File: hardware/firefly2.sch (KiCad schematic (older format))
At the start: 18 parts, among them J2 614105150721, J3 CONN_01X01, P3 CONN_01X04, P4 CONN_01X05, P5 CONN_01X01, U1 SAMD21E18, U2 RFM69CW, U3 MIC5504

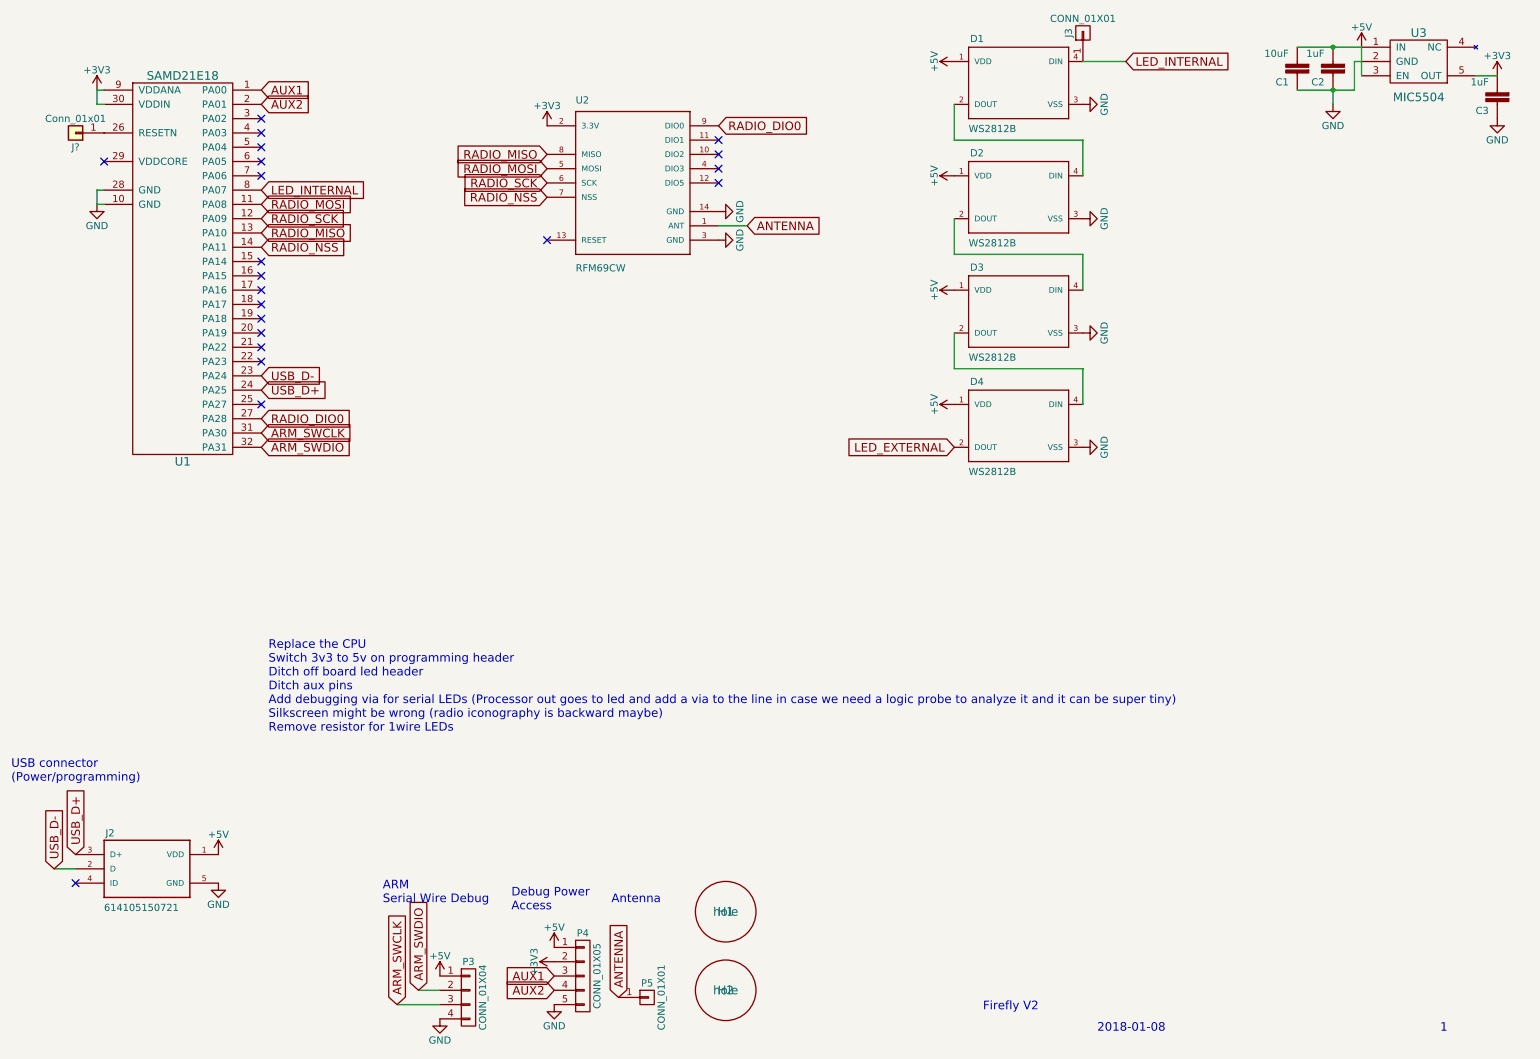
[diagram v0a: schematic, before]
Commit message: Hardware revision 2.4:
- Add buffer to bump LED signal to input voltage
- Add pads between reset and ground, to facilitate testing

Change-Id: If3ba1aed20585e03bd6f188c24cdaebd21a51b41
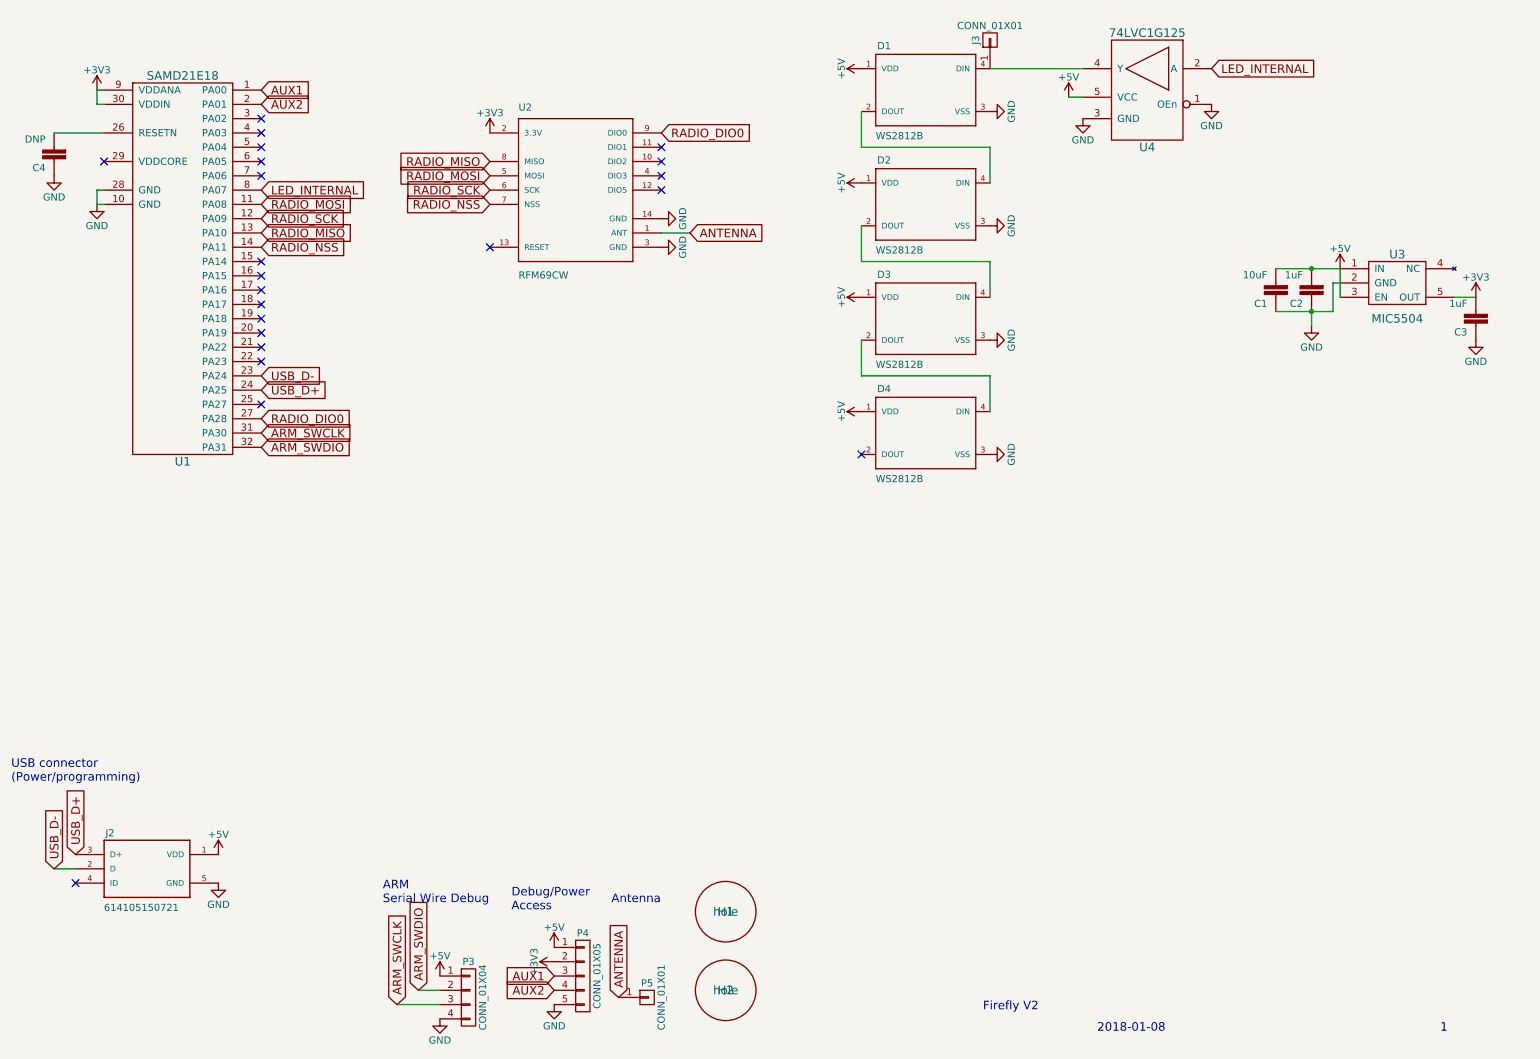
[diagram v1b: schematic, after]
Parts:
- removed J?: Conn_01x01, symbol Conn_01x01
- added C4: DNP, SparkFun-Capacitors:0603, symbol CAP0603-CAP
- added U4: 74LVC1G125, TO_SOT_Packages_SMD:SOT-353_SC-70-5, symbol 74LVC1G125
- J3: footprint (none) -> Pin_Headers:Pin_Header_Straight_1x01_Pitch1.27mm
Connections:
- net +5V: now also U4.5 (VCC)
- net GND: now also C4.1, U4.1 (OEn), U4.3 (GND)
- net LED_INTERNAL: now also U4.2 (A); no longer D1.4 (DIN), J3.1 (P1)
- net at U1.26 (RESETN): now also C4.2
- net LED_EXTERNAL: no longer names the net of D4.2 (DOUT)
- new net: D1.4 (DIN), J3.1 (P1), U4.4 (Y)
- no-connect marks 21 -> 22
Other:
- note added: "Debug/Power\nAccess"
- note removed: "Debug Power\nAccess"
- note removed: "Replace the CPU\nSwitch 3v3 to 5v on programming header\nDitch off board led header\nDitch aux pins\nAdd debugging via for serial LEDs (Processor out goes to led and add a via to the line in case we need a logic probe to analyze it and it can be super tiny)\nSilkscreen might be wrong (radio iconography is backward maybe)\nRemove resistor for 1wire LEDs\n"
- moved on the sheet: C1, C2, C3, D1, D2, D3, D4, J3, U2, U3

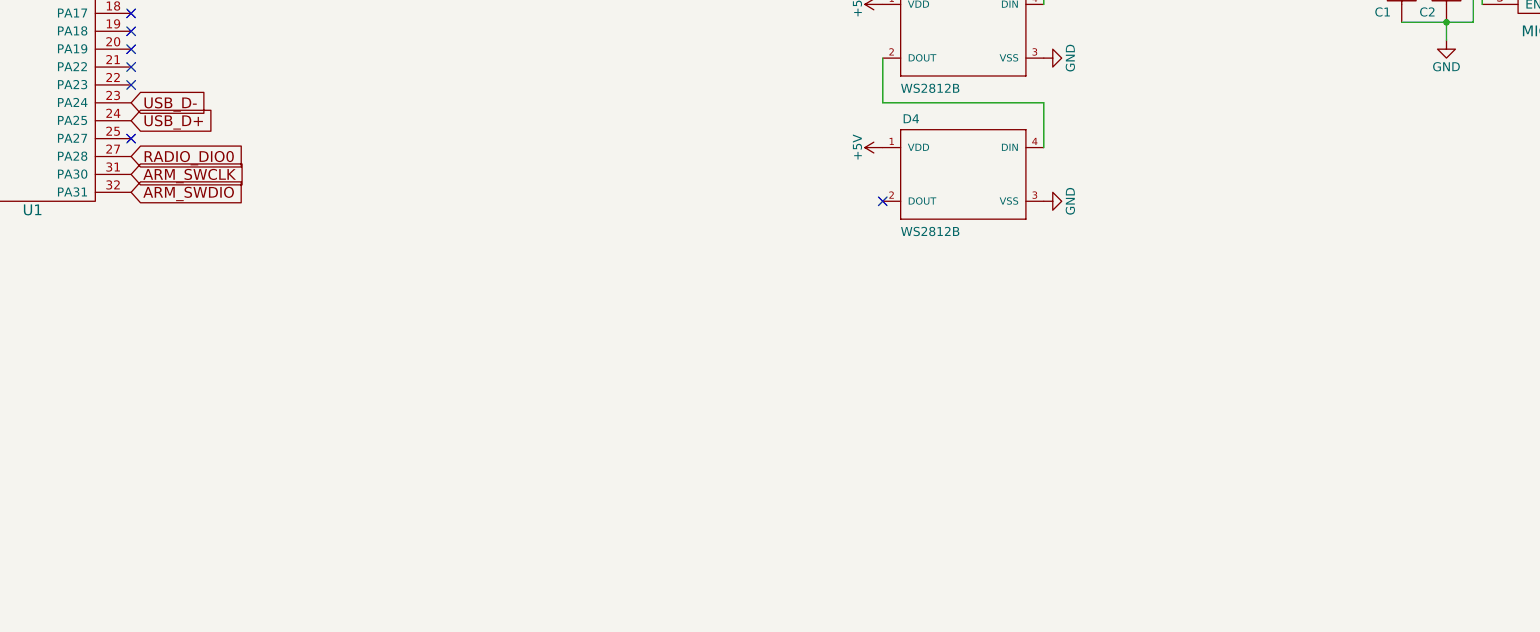
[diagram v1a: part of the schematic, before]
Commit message: Hard v2.5:
- Add a power eater circuit to keep USB batteries on

Change-Id: I22aef8479abf481f47f24733b5794af7d33fd833
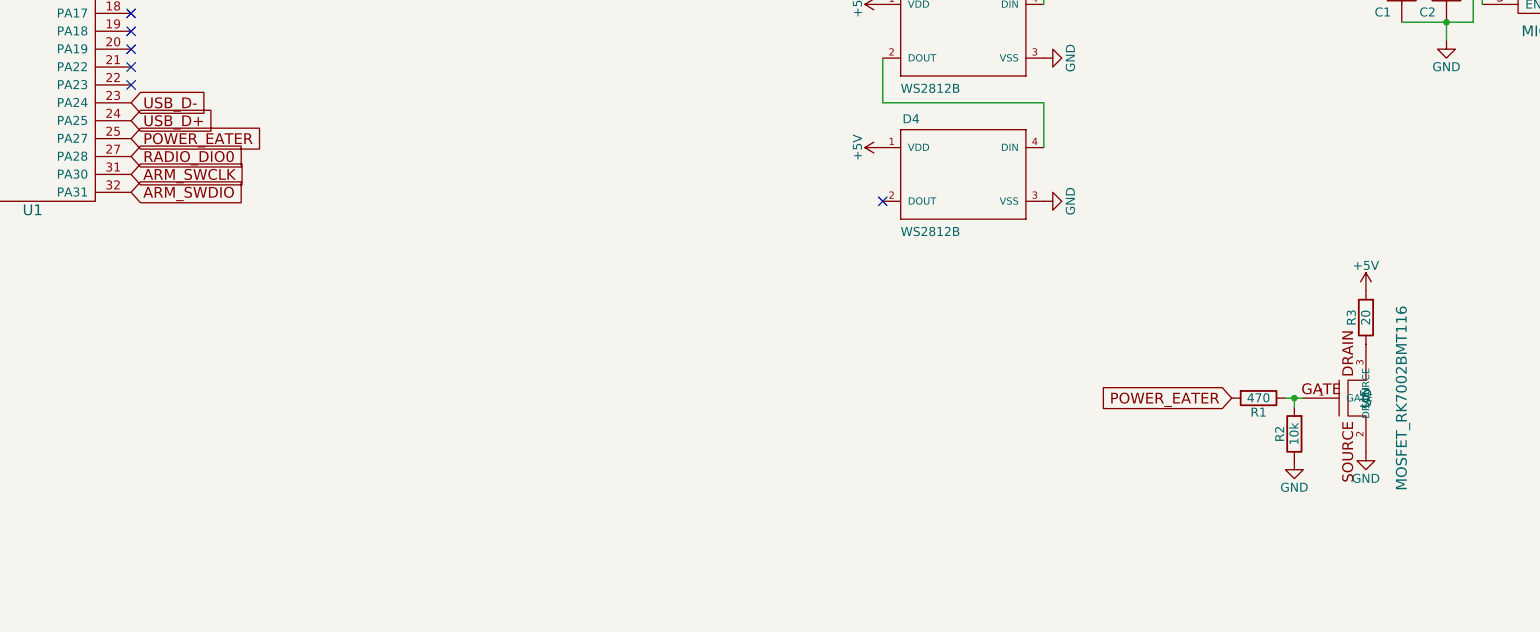
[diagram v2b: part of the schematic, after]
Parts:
- added R1: 470, Resistors_SMD:R_0603, symbol R
- added R2: 10k, Resistors_SMD:R_0603, symbol R
- added R3: 20, Resistors_SMD:R_0805, symbol R
- added U5: MOSFET_RK7002BMT116, TO_SOT_Packages_SMD:SOT-23, symbol MOSFET_RK7002BMT116
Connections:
- net +5V: now also R3.2
- net GND: now also R2.1, U5.2 (SOURCE)
- net POWER_EATER: now reaches U1.25 (PA27)
- net POWER_EATER: now also R1.2
- new net: R1.1, R2.2, U5.1 (GATE)
- new net: R3.1, U5.3 (DRAIN)
- no-connect marks 22 -> 21
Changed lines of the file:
@@
 NoConn ~ 2300 2850
 NoConn ~ 2300 2950
-NoConn ~ 2300 3250
 $Comp
 L +5V #PWR024
@@
 $EndComp
 NoConn ~ 6500 3600
+Text GLabel 2300 3250 2    60   Input ~ 0
+POWER_EATER
+Text GLabel 8450 4700 0    60   Input ~ 0
+POWER_EATER
+$Comp
+L GND #PWR029
+U 1 1 5B56927D
+P 9200 5000
+F 0 "#PWR029" H 9200 4750 50  0001 C CNN
+F 1 "GND" H 9200 4850 50  0000 C CNN
+F 2 "" H 9200 5000 50  0000 C CNN
+F 3 "" H 9200 5000 50  0000 C CNN
+	1    9200 5000
+	1    0    0    -1
+$EndComp
+$Comp
+L R R1
+U 1 1 5B569842
+P 8600 4700
+F 0 "R1" V 8680 4700 50  0000 C CNN
+F 1 "470" V 8600 4700 50  0000 C CNN
+F 2 "Resistors_SMD:R_0603" V 8530 4700 50  0001 C CNN
+F 3 "" H 8600 4700 50  0001 C CNN
+	1    8600 4700
+	0    1    1    0
+$EndComp
+$Comp
+L R R2
+U 1 1 5B569944
+P 8800 4900
+F 0 "R2" V 8880 4900 50  0000 C CNN
+F 1 "10k" V 8800 4900 50  0000 C CNN
+F 2 "Resistors_SMD:R_0603" V 8730 4900 50  0001 C CNN
+F 3 "" H 8800 4900 50  0001 C CNN
+	1    8800 4900
+	-1   0    0    1
+$EndComp
+$Comp
+L GND #PWR030
+U 1 1 5B5699AC
+P 8800 5050
+F 0 "#PWR030" H 8800 4800 50  0001 C CNN
+F 1 "GND" H 8800 4900 50  0000 C CNN
+F 2 "" H 8800 5050 50  0000 C CNN
+F 3 "" H 8800 5050 50  0000 C CNN
+	1    8800 5050
+	1    0    0    -1
+$EndComp
+Wire Wire Line
+	8850 4700 8750 4700
+Wire Wire Line
+	8800 4750 8800 4700
+Connection ~ 8800 4700
+$Comp
+L +5V #PWR031
+U 1 1 5B569D7A
+P 9200 4100
+F 0 "#PWR031" H 9200 3950 50  0001 C CNN
+F 1 "+5V" H 9200 4240 50  0000 C CNN
+F 2 "" H 9200 4100 50  0000 C CNN
+F 3 "" H 9200 4100 50  0000 C CNN
+	1    9200 4100
+	1    0    0    -1
+$EndComp
+$Comp
+L R R3
+U 1 1 5B569DC7
+P 9200 4250
+F 0 "R3" V 9280 4250 50  0000 C CNN
+F 1 "20" V 9200 4250 50  0000 C CNN
+F 2 "Resistors_SMD:R_0805" V 9130 4250 50  0001 C CNN
+F 3 "" H 9200 4250 50  0001 C CNN
+	1    9200 4250
+	-1   0    0    1
+$EndComp
+$Comp
+L MOSFET_RK7002BMT116 U5
+U 1 1 5B56A262
+P 9300 4700
+F 0 "U5" H 9300 4800 60  0000 C CNN
+F 1 "MOSFET_RK7002BMT116" H 9300 4600 60  0000 C CNN
+F 2 "TO_SOT_Packages_SMD:SOT-23" H 9300 4650 60  0001 C CNN
+F 3 "" H 9300 4650 60  0000 C CNN
+	1    9300 4700
+	0    -1   -1   0
+$EndComp
 $EndSCHEMATC
